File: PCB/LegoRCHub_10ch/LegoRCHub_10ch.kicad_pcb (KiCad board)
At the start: 2 copper layers, 39.3 x 55.2 mm, 41 parts, among them J1 Conn_01x02, J10 Conn_01x03, J11 Conn_01x03_MountingPin, J12 Conn_01x02, J13 Conn_01x01, J2 Conn_01x02, J3 Conn_01x02, J4 Conn_01x02, J5 Conn_01x02, J6 Conn_01x02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

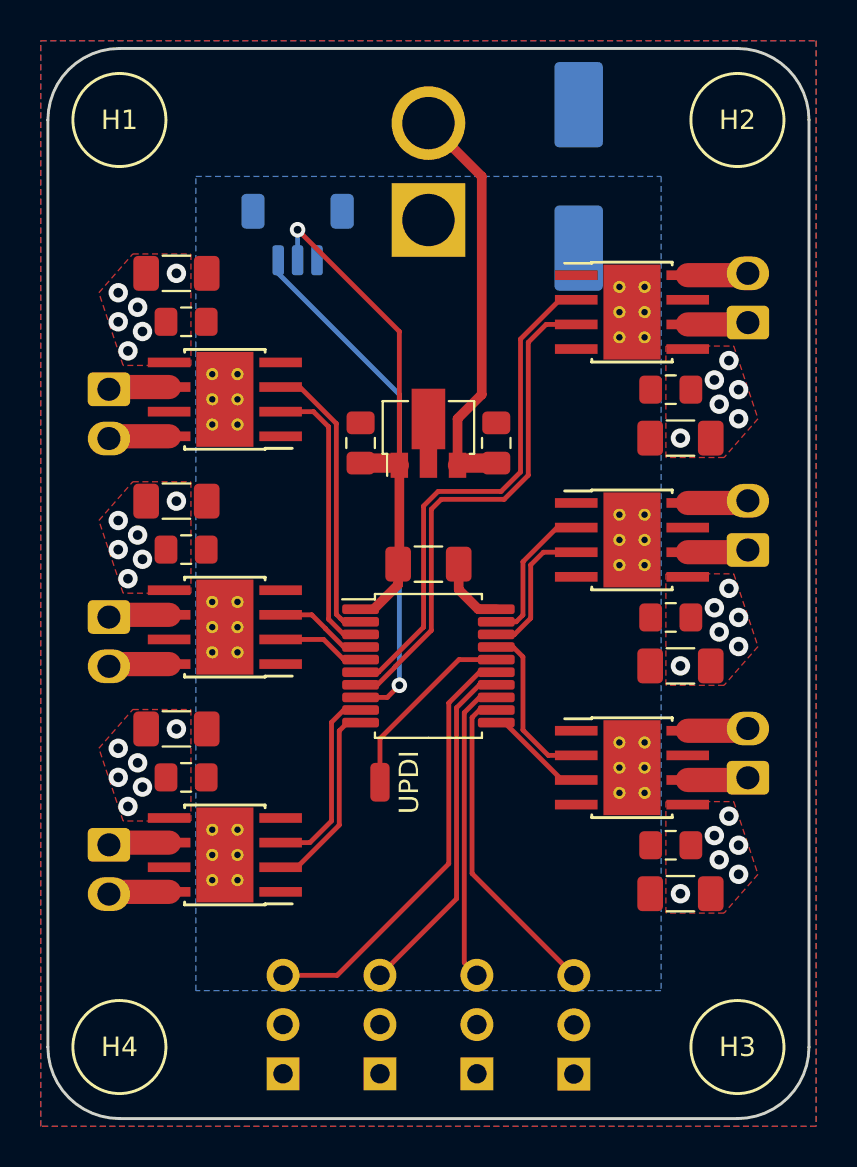
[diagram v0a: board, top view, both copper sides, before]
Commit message: LegoRCHub_10ch: improved layout...
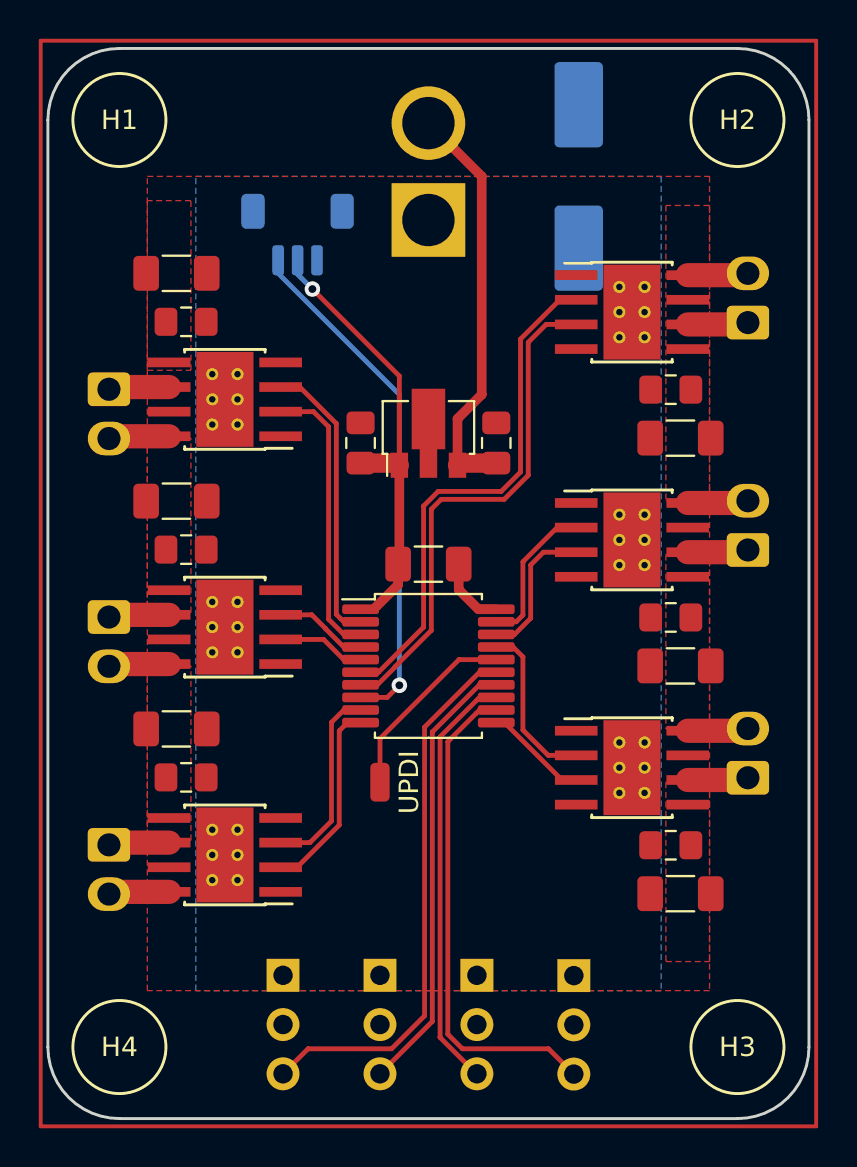
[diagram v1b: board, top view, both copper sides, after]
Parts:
- moved J10 5.08 mm to (47.0, 71.0), turned to 180 degrees
- moved J9 5.08 mm to (42.0, 71.0), turned to 180 degrees
- moved J7 5.08 mm to (37.0, 71.0), turned to 180 degrees
- moved J8 5.08 mm to (52.0, 71.0), turned to 180 degrees
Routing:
- net /CH8: track 16.9 -> 25.6 mm
- net /CH10: track 15.8 -> 21.9 mm
- net /CH7: track 22.3 -> 28.3 mm
- net /CH9: track 18.0 -> 23.1 mm
- net VCC: track 25.8 -> 22.7 mm
- net +BATT: vias 36 -> 0

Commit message: LegoRCHub_10ch: improved layout: beta-2
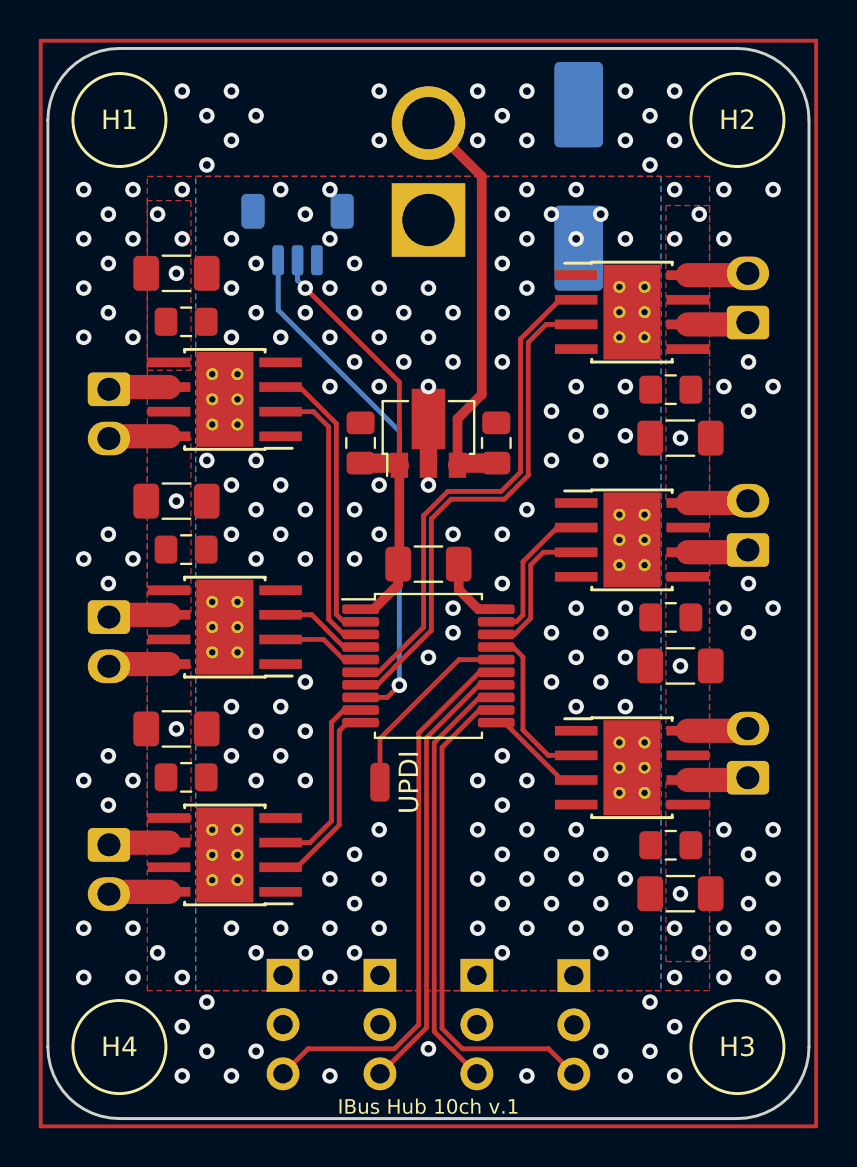
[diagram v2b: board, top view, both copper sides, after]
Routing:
- net GND: vias 0 -> 124
- net +BATT: vias 0 -> 94
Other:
- board text added: "IBus Hub 10ch v.1"

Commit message: LegoRCHub_10ch: improved layout: beta-3
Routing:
- net +BATT: vias 94 -> 96
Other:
- board text added: "Lego RC Hub 10ch v1"
- board text removed: "IBus Hub 10ch v.1"
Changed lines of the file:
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@@
   (paper "A4")
   (title_block
-    (title "IBus Hub 10ch v1")
+    (title "Lego RC Hub 10ch v1")
   )
   (layers
@@
     (effects (font (size 1 1) (thickness 0.15)))
   )
-  (gr_text "IBus Hub 10ch v.1" (at 44.45 77.8) (layer "F.SilkS")
+  (gr_text "Lego RC Hub 10ch v1" (at 44.45 77.8) (layer "F.SilkS")
     (effects (font (size 0.75 0.75) (thickness 0.1)))
   )
@@
   (via (at 60.96 39.37) (size 0.8) (drill 0.4) (layers "F.Cu" "B.Cu") (free) (net 2))
   (via (at 27.94 34.29) (size 0.8) (drill 0.4) (layers "F.Cu" "B.Cu") (free) (net 2))
+  (via (at 36.83 27.94) (size 0.8) (drill 0.4) (layers "F.Cu" "B.Cu") (free) (net 2))
   (via (at 30.48 69.85) (size 0.8) (drill 0.4) (layers "F.Cu" "B.Cu") (free) (net 2))
   (via (at 33.02 29.21) (size 0.8) (drill 0.4) (layers "F.Cu" "B.Cu") (free) (net 2))
@@
   (via (at 57.45 55.05) (size 0.8) (drill 0.4) (layers "F.Cu" "B.Cu") (free) (net 2))
   (via (at 54.61 27.94) (size 0.8) (drill 0.4) (layers "F.Cu" "B.Cu") (free) (net 2))
+  (via (at 36.83 25.4) (size 0.8) (drill 0.4) (layers "F.Cu" "B.Cu") (free) (net 2))
   (via (at 59.69 52.07) (size 0.8) (drill 0.4) (layers "F.Cu" "B.Cu") (free) (net 2))
   (via (at 30.48 31.75) (size 0.8) (drill 0.4) (layers "F.Cu" "B.Cu") (free) (net 2))
